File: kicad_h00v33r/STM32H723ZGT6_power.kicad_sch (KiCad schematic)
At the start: 17 parts, among them U1 STM32H723ZGT6

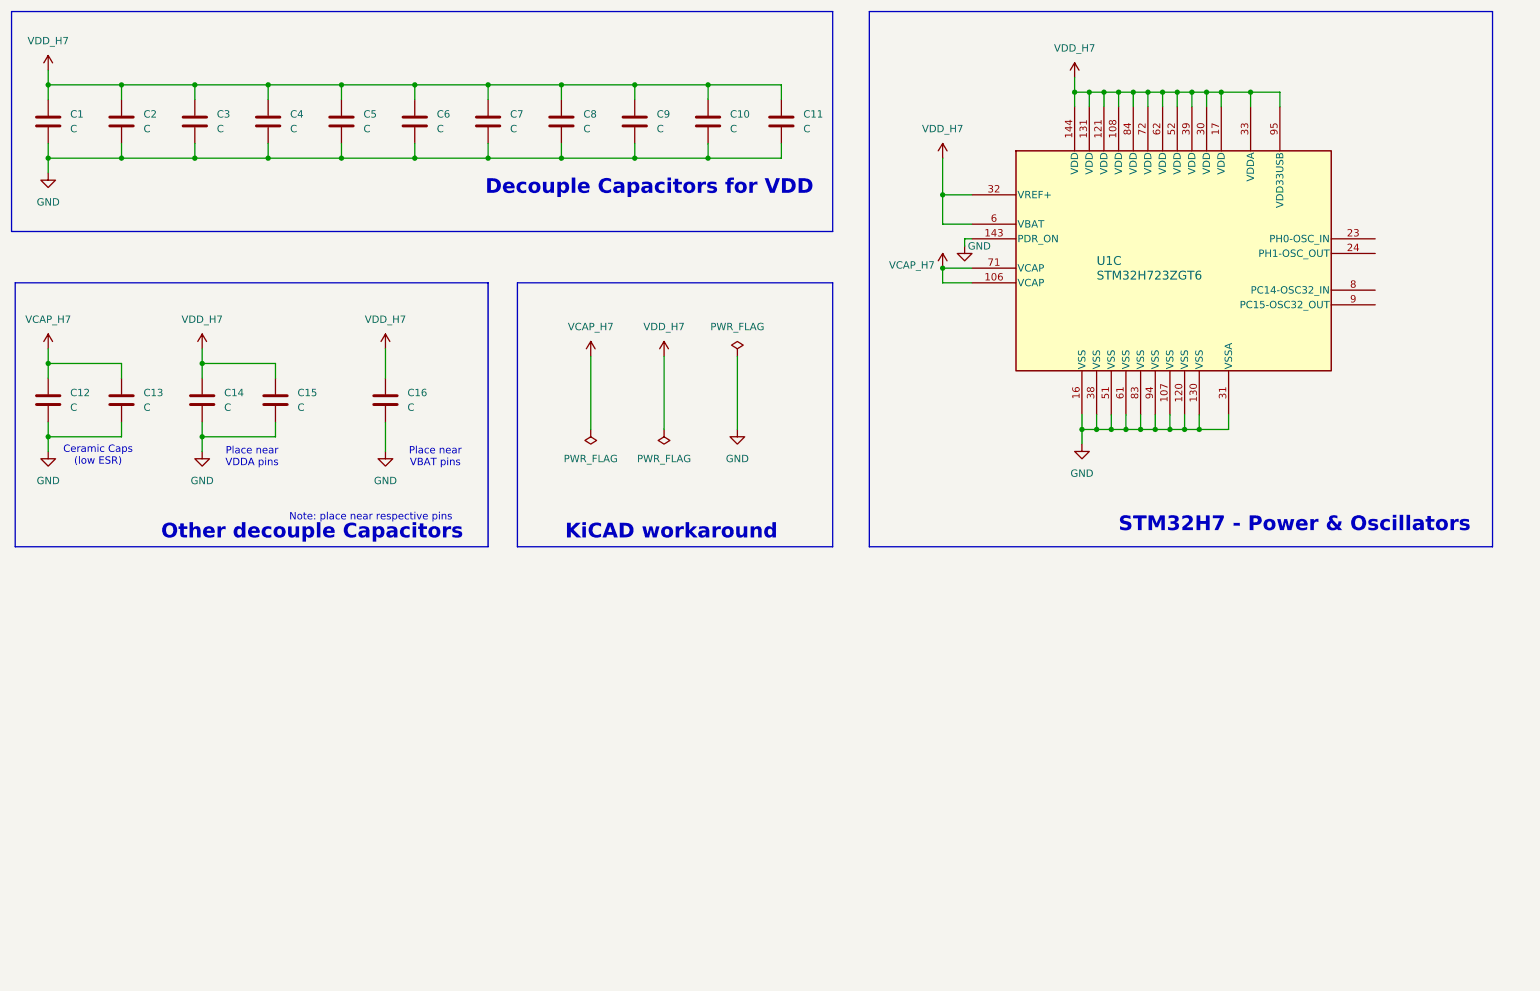
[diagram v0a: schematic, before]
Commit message: power supply + HSE completed
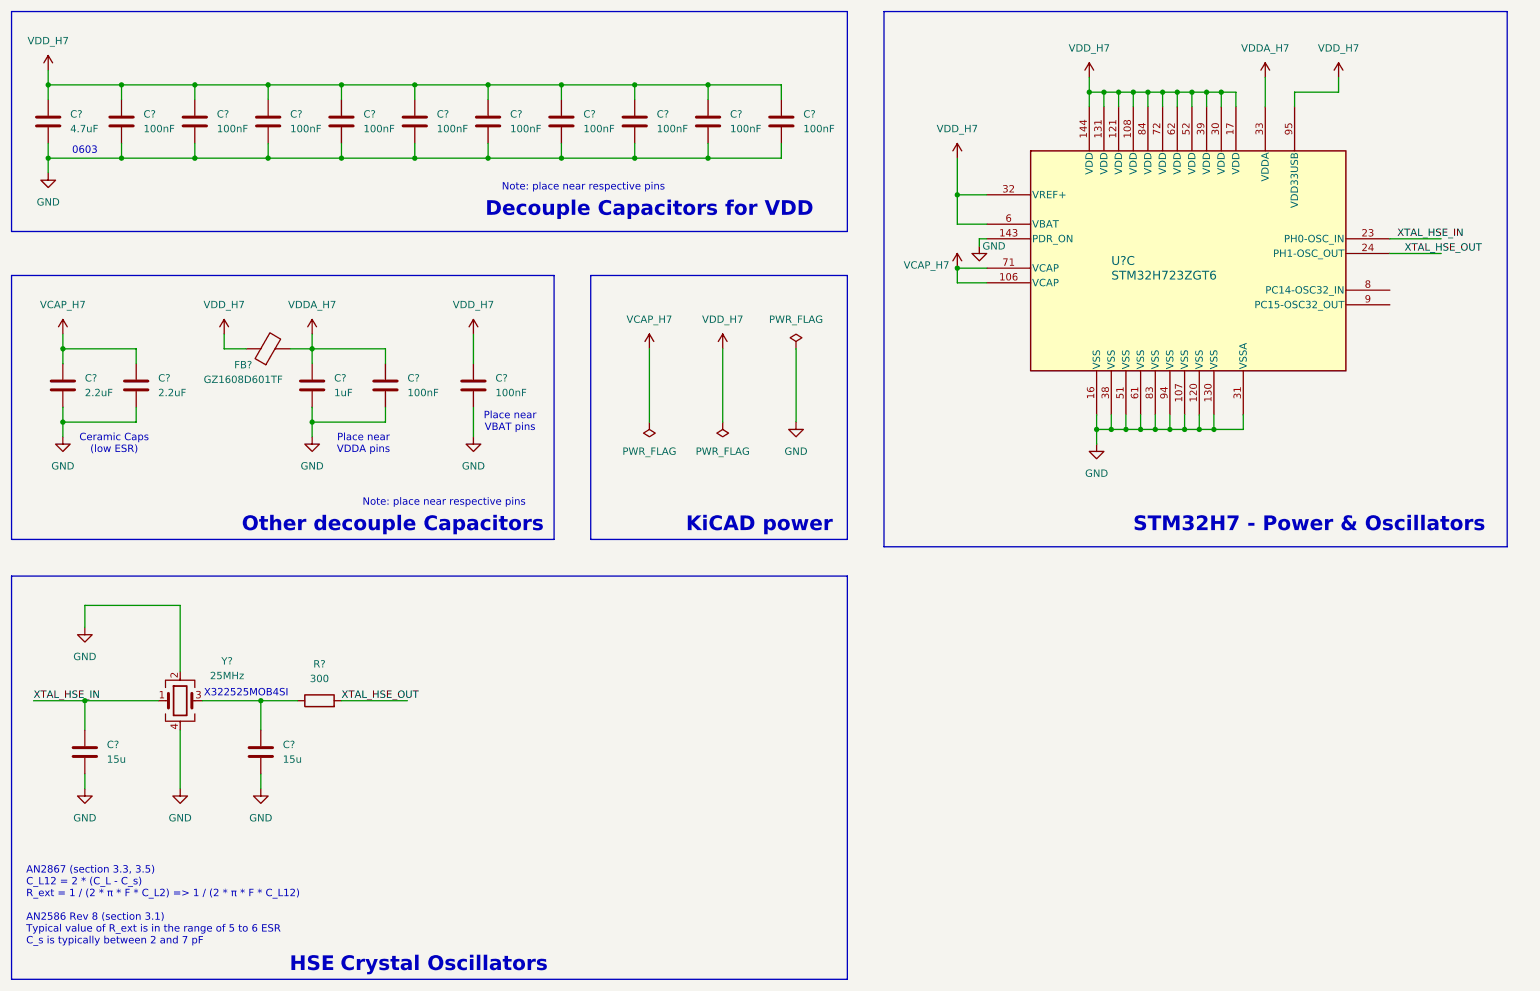
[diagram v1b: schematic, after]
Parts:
- added C? (x2): 15u, symbol Device:C
- added FB?: GZ1608D601TF, symbol Device:FerriteBead
- added R?: 300, symbol Device:R
- added Y?: 25MHz, symbol Device:Crystal_GND24
- C?: renamed from C15; value C -> 100nF
- C?: renamed from C10; value C -> 100nF
- C?: renamed from C7; value C -> 100nF
- C?: renamed from C11; value C -> 100nF
- C?: renamed from C1; value C -> 4.7uF
- C?: renamed from C5; value C -> 100nF
- C?: renamed from C12; value C -> 2.2uF
- C?: renamed from C6; value C -> 100nF
- C?: renamed from C14; value C -> 1uF
- C?: renamed from C4; value C -> 100nF
- C?: renamed from C8; value C -> 100nF
- C?: renamed from C9; value C -> 100nF
- C?: renamed from C13; value C -> 2.2uF
- C?: renamed from C16; value C -> 100nF
- C?: renamed from C2; value C -> 100nF
- C?: renamed from C3; value C -> 100nF
- renumbered U1 to U?
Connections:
- net GND: now also C?.2, C?.2, Y?.2, Y?.4
- net VDD_H7: now also FB?.1; no longer C?.1, C?.1, U?.33 (VDDA)
- net XTAL_HSE_IN: now reaches U?.23 (PH0-OSC_IN)
- net XTAL_HSE_IN: now also C?.1, Y?.1
- net XTAL_HSE_OUT: now reaches U?.24 (PH1-OSC_OUT)
- net XTAL_HSE_OUT: now also R?.2
- new net: C?.1, R?.1, Y?.3
- new net VDDA_H7: C?.1, C?.1, FB?.2, U?.33 (VDDA)
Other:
- note added: "0603"
- note added: "AN2867 (section 3.3, 3.5) C_L12 = 2 * (C_L - C_s) R_ext = 1 / (2 * π * F * C_L2) => 1 / (2 * π * F * C_L12) AN2586 Rev 8 (section 3.1) Typical value of R_ext is in the range of 5 to 6 ESR C_s is typically between 2 and 7 pF"
- note added: "Crystal Oscillators"
- note added: "HSE"
- note added: "KiCAD power"
- note added: "X322525MOB4SI"
- note removed: "KiCAD workaround"
- moved on the sheet: C?, U?C
